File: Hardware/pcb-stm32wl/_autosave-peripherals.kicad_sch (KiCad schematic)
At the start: 52 parts, among them J10 Qwiic, J11 Conn_02x08_Odd_Even, J13 Conn_02x08_Odd_Even, J8 DEBUG, J9 UART/I2C, Q2 PMST4401,115, SW1 USR_BTN, SW2 RESET, U10 SHTC3, U3 AD7124-8BCPZ-RL7, U6 ICM-42605, U7 MRF89XAM9AT-I/RM

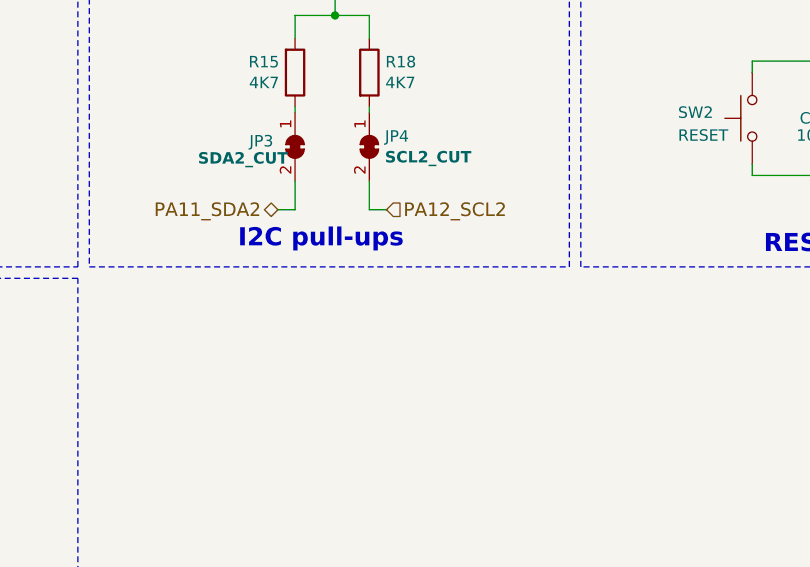
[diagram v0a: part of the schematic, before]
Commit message: power circuitry completely wired
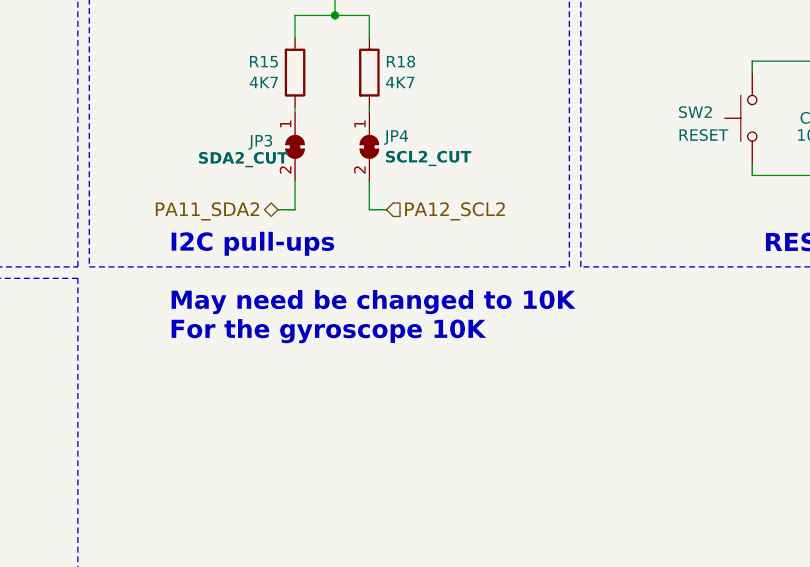
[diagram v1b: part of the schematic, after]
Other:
- note added: "I2C pull-ups May need be changed to 10K For the gyroscope 10K"
- note removed: "I2C pull-ups"
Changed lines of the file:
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@@
 		)
 	)
-	(text "I2C pull-ups"
+	(text "I2C pull-ups\n\nMay need be changed to 10K\nFor the gyroscope 10K"
 		(exclude_from_sim no)
-		(at 179.07 136.525 0)
+		(at 171.45 146.812 0)
 		(effects
 			(font

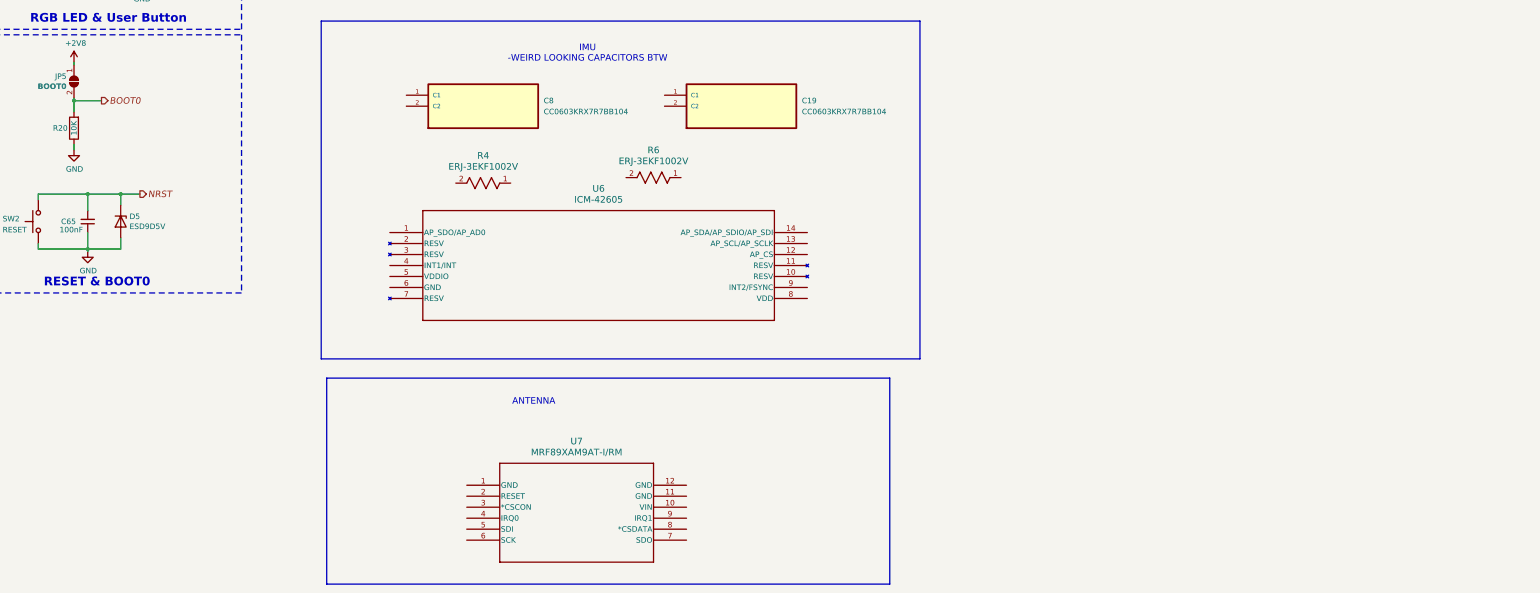
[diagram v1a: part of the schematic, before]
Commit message: wired, and selected capacitors. Not sure if they are correct as there was nothing in datasheet for it
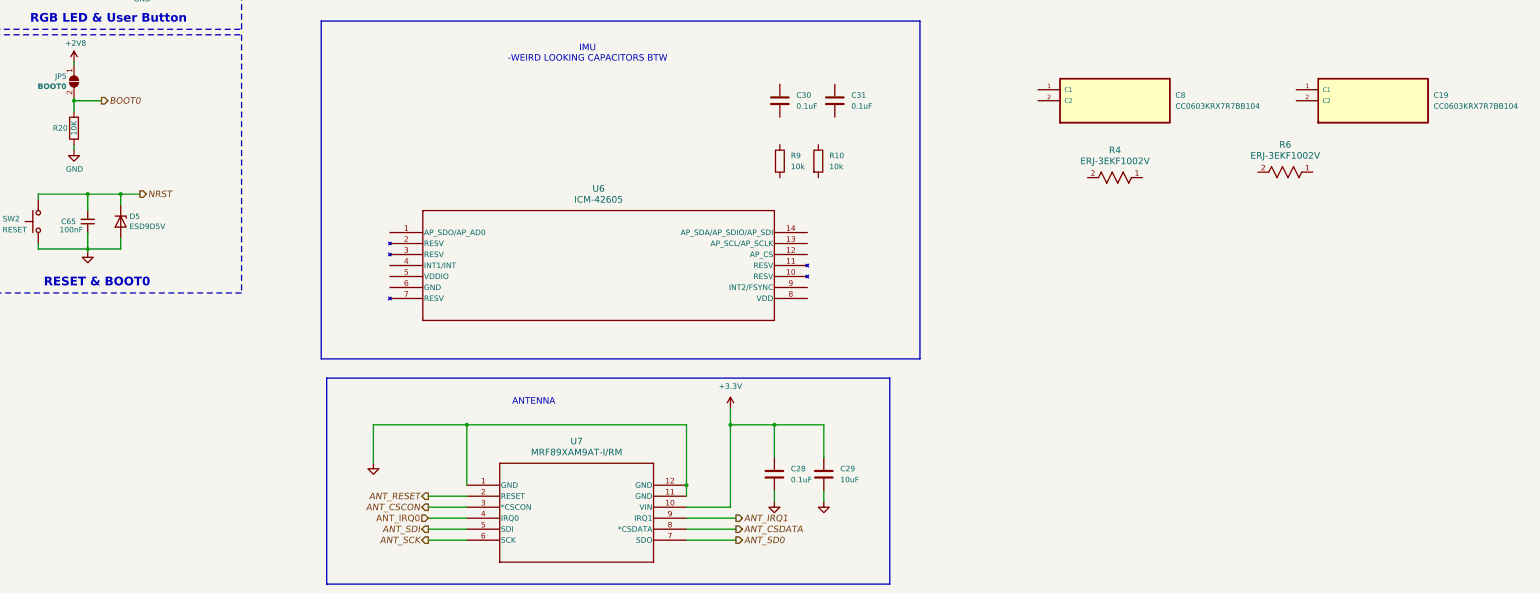
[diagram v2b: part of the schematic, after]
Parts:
- added C28, C30, C31: 0.1uF, Capacitor_SMD:C_0402_1005Metric, symbol Device:C
- added C29: 10uF, Capacitor_SMD:C_1206_3216Metric, symbol Device:C
- added R10, R9: 10k, symbol Device:R
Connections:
- net GND: now also U7.1 (GND), U7.11 (GND), U7.12 (GND), C28.2, C29.2
- net +3.3V: now reaches U7.10 (VIN)
- net +3.3V: now also C28.1, C29.1
- net ANT_RESET: now reaches U7.2 (RESET)
- net ANT_CSCON: now reaches U7.3 (*CSCON)
- net ANT_IRQ0: now reaches U7.4 (IRQ0)
- net ANT_SDI: now reaches U7.5 (SDI)
- net ANT_SCK: now reaches U7.6 (SCK)
- net ANT_SD0: now reaches U7.7 (SDO)
- net ANT_CSDATA: now reaches U7.8 (*CSDATA)
- net ANT_IRQ1: now reaches U7.9 (IRQ1)
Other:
- moved on the sheet: C19, C8, R4, R6
